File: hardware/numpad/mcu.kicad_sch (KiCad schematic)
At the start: 6 parts

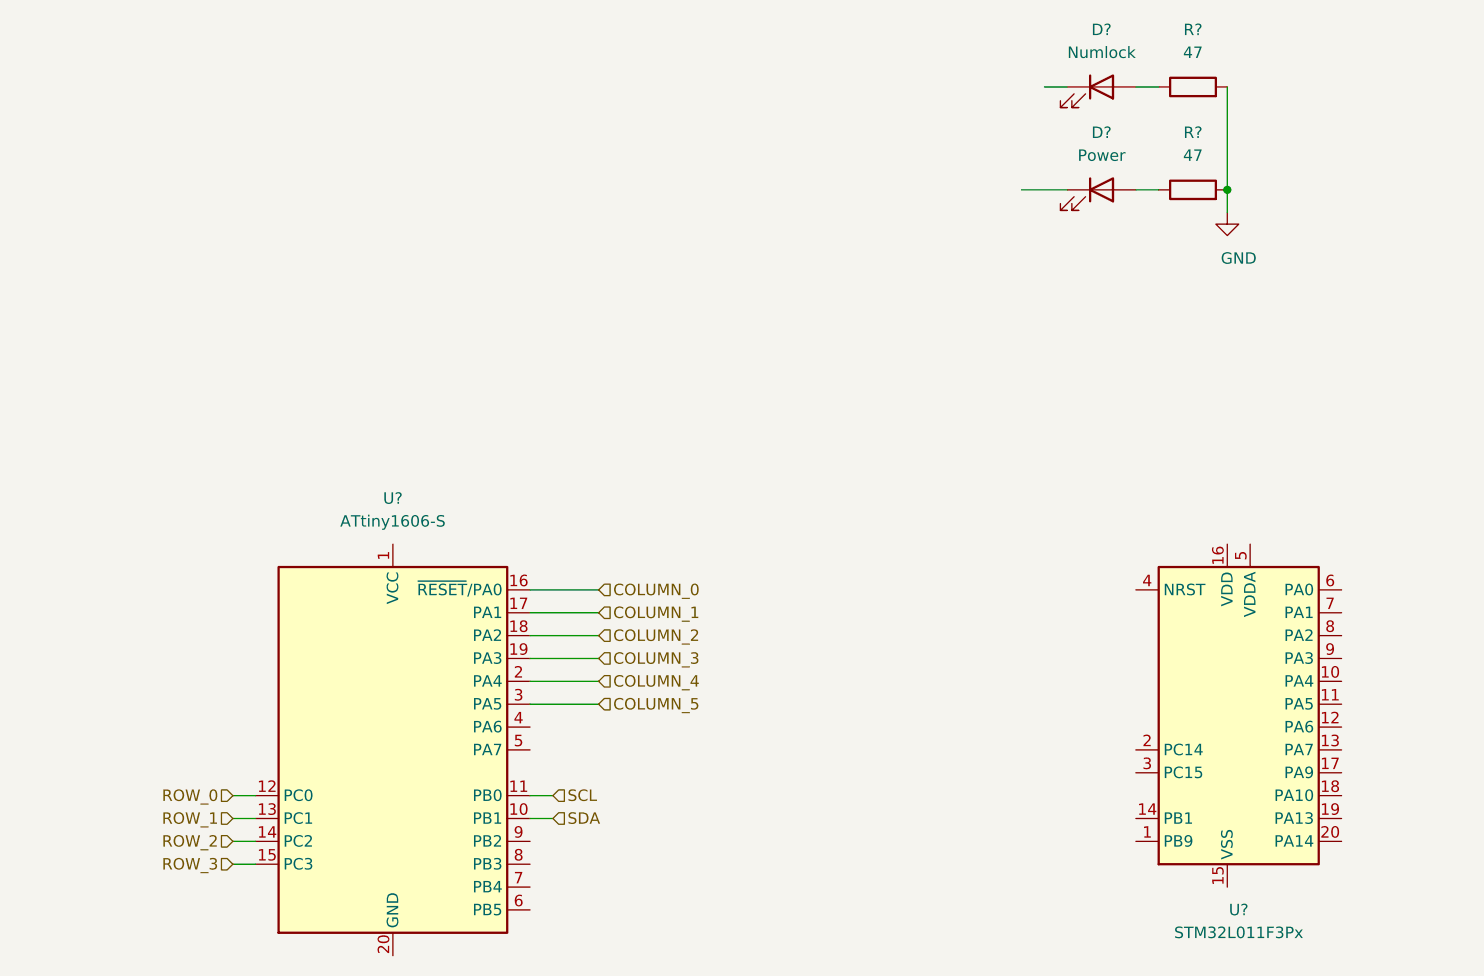
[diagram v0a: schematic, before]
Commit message: Exchange the ATtiny with a STM32L011F4P6 for the numpad
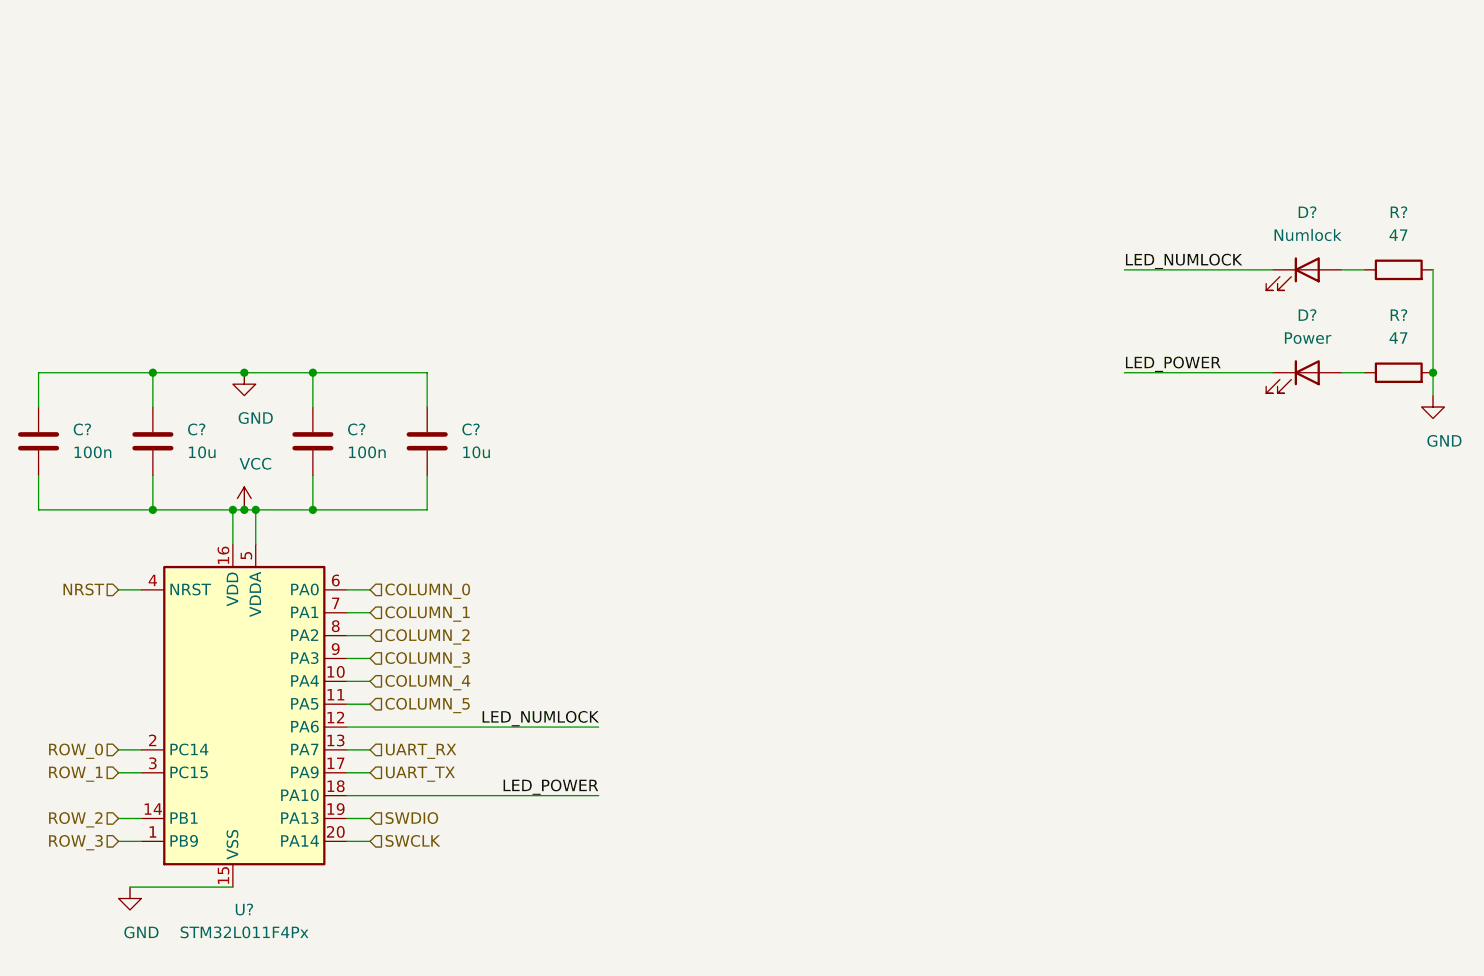
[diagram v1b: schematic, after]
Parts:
- removed U?: ATtiny1606-S, Package_SO:SOIC-20W_7.5x12.8mm_P1.27mm, symbol MCU_Microchip_ATtiny:ATtiny1606-S
- removed U?: STM32L011F3Px, Package_SO:TSSOP-20_4.4x6.5mm_P0.65mm, symbol MCU_ST_STM32L0:STM32L011F3Px
- added C? (x2): 10u, symbol Device:C
- added C? (x2): 100n, symbol Device:C
- added U?: STM32L011F4Px, Package_SO:TSSOP-20_4.4x6.5mm_P0.65mm, symbol MCU_ST_STM32L0:STM32L011F4Px
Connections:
- net COLUMN_0: now also U?.6 (PA0)
- net COLUMN_1: now also U?.7 (PA1)
- net COLUMN_2: now also U?.8 (PA2)
- net COLUMN_3: now also U?.9 (PA3)
- net COLUMN_4: now also U?.10 (PA4)
- net COLUMN_5: now also U?.11 (PA5)
- net GND: now also C?.1, C?.1, C?.1, C?.1, U?.15 (VSS)
- net ROW_0: now also U?.2 (PC14)
- net ROW_1: now also U?.3 (PC15)
- net ROW_2: now also U?.14 (PB1)
- net ROW_3: now also U?.1 (PB9)
- net LED_POWER: now reaches D?.1 (K)
- net LED_POWER: now also U?.18 (PA10)
- net LED_NUMLOCK: now reaches D?.1 (K)
- net LED_NUMLOCK: now also U?.12 (PA6)
- new net NRST: U?.4 (NRST)
- new net SWCLK: U?.20 (PA14)
- new net SWDIO: U?.19 (PA13)
- new net UART_RX: U?.13 (PA7)
- new net UART_TX: U?.17 (PA9)
- new net VCC: C?.2, C?.2, C?.2, C?.2, U?.16 (VDD), U?.5 (VDDA)
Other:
- moved on the sheet: D?, R?

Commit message: Remove UART line from the NRF to the numpad
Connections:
- net UART_RX: no longer names the net of U?.13 (PA7)
- no-connect marks 0 -> 1
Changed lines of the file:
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@@
   (junction (at 110.49 81.28) (diameter 0.9144) (color 0 0 0 0))
   (junction (at 234.95 66.04) (diameter 0.9144) (color 0 0 0 0))
+  (no_connect (at 114.3 107.95))
   (wire (pts (xy 80.01 66.04) (xy 80.01 69.85))
     (stroke (width 0) (type solid) (color 0 0 0 0))
@@
     (stroke (width 0) (type solid) (color 0 0 0 0))
   )
-  (wire (pts (xy 114.3 107.95) (xy 116.84 107.95))
-    (stroke (width 0) (type solid) (color 0 0 0 0))
-  )
   (wire (pts (xy 114.3 110.49) (xy 116.84 110.49))
     (stroke (width 0) (type solid) (color 0 0 0 0))
@@
     (effects (font (size 1.27 1.27)) (justify left))
   )
-  (hierarchical_label "UART_RX" (shape input) (at 116.84 107.95 0)
-    (effects (font (size 1.27 1.27)) (justify left))
-  )

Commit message: Add a line for the UART direction main->numpad
This is necessary as the numlock-led is situated on the numpad and the
main mcu has to be able to switch it on and off.
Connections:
- net LED_POWER: now also U?.13 (PA7); no longer U?.18 (PA10)
- new net UART_RX: U?.18 (PA10)
- no-connect marks 1 -> 0
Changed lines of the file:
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@@
   (junction (at 110.49 81.28) (diameter 0.9144) (color 0 0 0 0))
   (junction (at 234.95 66.04) (diameter 0.9144) (color 0 0 0 0))
-  (no_connect (at 114.3 107.95))
   (wire (pts (xy 80.01 66.04) (xy 80.01 69.85))
     (stroke (width 0) (type solid) (color 0 0 0 0))
@@
     (stroke (width 0) (type solid) (color 0 0 0 0))
   )
+  (wire (pts (xy 114.3 113.03) (xy 116.84 113.03))
+    (stroke (width 0) (type solid) (color 0 0 0 0))
+  )
   (wire (pts (xy 114.3 115.57) (xy 116.84 115.57))
     (stroke (width 0) (type solid) (color 0 0 0 0))
@@
     (stroke (width 0) (type solid) (color 0 0 0 0))
   )
-  (wire (pts (xy 142.24 113.03) (xy 114.3 113.03))
+  (wire (pts (xy 142.24 107.95) (xy 114.3 107.95))
     (stroke (width 0) (type solid) (color 0 0 0 0))
   )
@@
     (effects (font (size 1.27 1.27)) (justify right bottom))
   )
-  (label "LED_POWER" (at 142.24 113.03 180)
+  (label "LED_POWER" (at 142.24 107.95 180)
     (effects (font (size 1.27 1.27)) (justify right bottom))
   )
@@
     (effects (font (size 1.27 1.27)) (justify left))
   )
+  (hierarchical_label "UART_RX" (shape input) (at 116.84 113.03 0)
+    (effects (font (size 1.27 1.27)) (justify left))
+  )

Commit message: Add first rough version of the numpad PCB
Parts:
- C2, C3, C4, C5: renamed from C?; footprint (none) -> Capacitor_SMD:C_0603_1608Metric_Pad1.08x0.95mm_HandSolder
- D11, D12: renamed from D?; footprint (none) -> Diode_SMD:D_0603_1608Metric_Pad1.05x0.95mm_HandSolder
- R1, R2: renamed from R?; footprint (none) -> Resistor_SMD:R_0603_1608Metric_Pad0.98x0.95mm_HandSolder
- gave numbers to parts that had none: 1
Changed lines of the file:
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@@
   (symbol (lib_id "power:VCC") (at 102.87 81.28 0) (unit 1)
     (in_bom yes) (on_board yes)
-    (property "Reference" "#PWR?" (id 0) (at 102.87 85.09 0)
+    (property "Reference" "#PWR0109" (id 0) (at 102.87 85.09 0)
       (effects (font (size 1.27 1.27)) hide)
     )
@@
   (symbol (lib_id "power:GND") (at 90.17 123.19 0) (unit 1)
     (in_bom yes) (on_board yes)
-    (property "Reference" "#PWR?" (id 0) (at 90.17 129.54 0)
+    (property "Reference" "#PWR0111" (id 0) (at 90.17 129.54 0)
       (effects (font (size 1.27 1.27)) hide)
     )
@@
   (symbol (lib_id "power:GND") (at 102.87 66.04 0) (unit 1)
     (in_bom yes) (on_board yes)
-    (property "Reference" "#PWR?" (id 0) (at 102.87 72.39 0)
+    (property "Reference" "#PWR0110" (id 0) (at 102.87 72.39 0)
       (effects (font (size 1.27 1.27)) hide)
     )
@@
   (symbol (lib_id "power:GND") (at 234.95 68.58 0) (unit 1)
     (in_bom yes) (on_board yes)
-    (property "Reference" "#PWR?" (id 0) (at 234.95 74.93 0)
+    (property "Reference" "#PWR0112" (id 0) (at 234.95 74.93 0)
       (effects (font (size 1.27 1.27)) hide)
     )
@@
   (symbol (lib_id "Device:R") (at 231.14 54.61 90) (unit 1)
     (in_bom yes) (on_board yes)
-    (property "Reference" "R?" (id 0) (at 231.14 48.26 90))
+    (property "Reference" "R1" (id 0) (at 231.14 48.26 90))
     (property "Value" "47" (id 1) (at 231.14 50.8 90))
-    (property "Footprint" "" (id 2) (at 231.14 56.388 90)
+    (property "Footprint" "Resistor_SMD:R_0603_1608Metric_Pad0.98x0.95mm_HandSolder" (id 2) (at 231.14 56.388 90)
       (effects (font (size 1.27 1.27)) hide)
     )
@@
   (symbol (lib_id "Device:R") (at 231.14 66.04 90) (unit 1)
     (in_bom yes) (on_board yes)
-    (property "Reference" "R?" (id 0) (at 231.14 59.69 90))
+    (property "Reference" "R2" (id 0) (at 231.14 59.69 90))
     (property "Value" "47" (id 1) (at 231.14 62.23 90))
-    (property "Footprint" "" (id 2) (at 231.14 67.818 90)
+    (property "Footprint" "Resistor_SMD:R_0603_1608Metric_Pad0.98x0.95mm_HandSolder" (id 2) (at 231.14 67.818 90)
       (effects (font (size 1.27 1.27)) hide)
     )
@@
   (symbol (lib_id "Device:LED") (at 220.98 54.61 0) (unit 1)
     (in_bom yes) (on_board yes)
-    (property "Reference" "D?" (id 0) (at 220.98 48.26 0))
+    (property "Reference" "D11" (id 0) (at 220.98 48.26 0))
     (property "Value" "Numlock" (id 1) (at 220.98 50.8 0))
-    (property "Footprint" "" (id 2) (at 220.98 54.61 0)
+    (property "Footprint" "Diode_SMD:D_0603_1608Metric_Pad1.05x0.95mm_HandSolder" (id 2) (at 220.98 54.61 0)
       (effects (font (size 1.27 1.27)) hide)
     )
@@
   (symbol (lib_id "Device:LED") (at 220.98 66.04 0) (unit 1)
     (in_bom yes) (on_board yes)
-    (property "Reference" "D?" (id 0) (at 220.98 59.69 0))
+    (property "Reference" "D12" (id 0) (at 220.98 59.69 0))
     (property "Value" "Power" (id 1) (at 220.98 62.23 0))
-    (property "Footprint" "" (id 2) (at 220.98 66.04 0)
+    (property "Footprint" "Diode_SMD:D_0603_1608Metric_Pad1.05x0.95mm_HandSolder" (id 2) (at 220.98 66.04 0)
       (effects (font (size 1.27 1.27)) hide)
     )
@@
   (symbol (lib_id "Device:C") (at 80.01 73.66 0) (unit 1)
     (in_bom yes) (on_board yes)
-    (property "Reference" "C?" (id 0) (at 83.82 72.39 0)
+    (property "Reference" "C2" (id 0) (at 83.82 72.39 0)
       (effects (font (size 1.27 1.27)) (justify left))
     )
@@
       (effects (font (size 1.27 1.27)) (justify left))
     )
-    (property "Footprint" "" (id 2) (at 80.9752 77.47 0)
+    (property "Footprint" "Capacitor_SMD:C_0603_1608Metric_Pad1.08x0.95mm_HandSolder" (id 2) (at 80.9752 77.47 0)
       (effects (font (size 1.27 1.27)) hide)
     )
@@
   (symbol (lib_id "Device:C") (at 92.71 73.66 0) (unit 1)
     (in_bom yes) (on_board yes)
-    (property "Reference" "C?" (id 0) (at 96.52 72.39 0)
+    (property "Reference" "C3" (id 0) (at 96.52 72.39 0)
       (effects (font (size 1.27 1.27)) (justify left))
     )
@@
       (effects (font (size 1.27 1.27)) (justify left))
     )
-    (property "Footprint" "" (id 2) (at 93.6752 77.47 0)
+    (property "Footprint" "Capacitor_SMD:C_0603_1608Metric_Pad1.08x0.95mm_HandSolder" (id 2) (at 93.6752 77.47 0)
       (effects (font (size 1.27 1.27)) hide)
     )
@@
   (symbol (lib_id "Device:C") (at 110.49 73.66 0) (unit 1)
     (in_bom yes) (on_board yes)
-    (property "Reference" "C?" (id 0) (at 114.3 72.39 0)
+    (property "Reference" "C4" (id 0) (at 114.3 72.39 0)
       (effects (font (size 1.27 1.27)) (justify left))
     )
@@
       (effects (font (size 1.27 1.27)) (justify left))
     )
-    (property "Footprint" "" (id 2) (at 111.4552 77.47 0)
+    (property "Footprint" "Capacitor_SMD:C_0603_1608Metric_Pad1.08x0.95mm_HandSolder" (id 2) (at 111.4552 77.47 0)
       (effects (font (size 1.27 1.27)) hide)
     )
@@
   (symbol (lib_id "Device:C") (at 123.19 73.66 0) (unit 1)
     (in_bom yes) (on_board yes)
-    (property "Reference" "C?" (id 0) (at 127 72.39 0)
+    (property "Reference" "C5" (id 0) (at 127 72.39 0)
       (effects (font (size 1.27 1.27)) (justify left))
     )
@@
       (effects (font (size 1.27 1.27)) (justify left))
     )
-    (property "Footprint" "" (id 2) (at 124.1552 77.47 0)
+    (property "Footprint" "Capacitor_SMD:C_0603_1608Metric_Pad1.08x0.95mm_HandSolder" (id 2) (at 124.1552 77.47 0)
       (effects (font (size 1.27 1.27)) hide)
     )
@@
   (symbol (lib_id "MCU_ST_STM32L0:STM32L011F4Px") (at 104.14 102.87 0) (unit 1)
     (in_bom yes) (on_board yes)
-    (property "Reference" "U?" (id 0) (at 102.87 125.73 0))
+    (property "Reference" "U1" (id 0) (at 102.87 125.73 0))
     (property "Value" "STM32L011F4Px" (id 1) (at 102.87 128.27 0))
     (property "Footprint" "Package_SO:TSSOP-20_4.4x6.5mm_P0.65mm" (id 2) (at 93.98 120.65 0)

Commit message: Numpad: exchange key identifer
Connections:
- net COLUMN_5: no longer names the net of U1.11 (PA5)
- no-connect marks 0 -> 1
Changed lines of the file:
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@@
   (junction (at 110.49 81.28) (diameter 0.9144) (color 0 0 0 0))
   (junction (at 234.95 66.04) (diameter 0.9144) (color 0 0 0 0))
+  (no_connect (at 114.3 102.87))
   (wire (pts (xy 80.01 66.04) (xy 80.01 69.85))
     (stroke (width 0) (type solid) (color 0 0 0 0))
@@
     (stroke (width 0) (type solid) (color 0 0 0 0))
   )
-  (wire (pts (xy 114.3 102.87) (xy 116.84 102.87))
-    (stroke (width 0) (type solid) (color 0 0 0 0))
-  )
   (wire (pts (xy 114.3 110.49) (xy 116.84 110.49))
     (stroke (width 0) (type solid) (color 0 0 0 0))
@@
     (effects (font (size 1.27 1.27)) (justify left))
   )
-  (hierarchical_label "COLUMN_5" (shape input) (at 116.84 102.87 0)
-    (effects (font (size 1.27 1.27)) (justify left))
-  )

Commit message: Numpad: WIP: design PCB
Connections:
- net LED_NUMLOCK: now also U1.13 (PA7); no longer U1.12 (PA6)
- net LED_POWER: now also U1.12 (PA6); no longer U1.13 (PA7)
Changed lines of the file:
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@@
     (stroke (width 0) (type solid) (color 0 0 0 0))
   )
-  (label "LED_NUMLOCK" (at 142.24 105.41 180)
+  (label "LED_POWER" (at 142.24 105.41 180)
     (effects (font (size 1.27 1.27)) (justify right bottom))
   )
-  (label "LED_POWER" (at 142.24 107.95 180)
+  (label "LED_NUMLOCK" (at 142.24 107.95 180)
     (effects (font (size 1.27 1.27)) (justify right bottom))
   )
